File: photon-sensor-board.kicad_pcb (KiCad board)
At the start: 2 copper layers, 35 x 50 mm, 4 parts, among them U1 PHOTON, U2 DS18B20

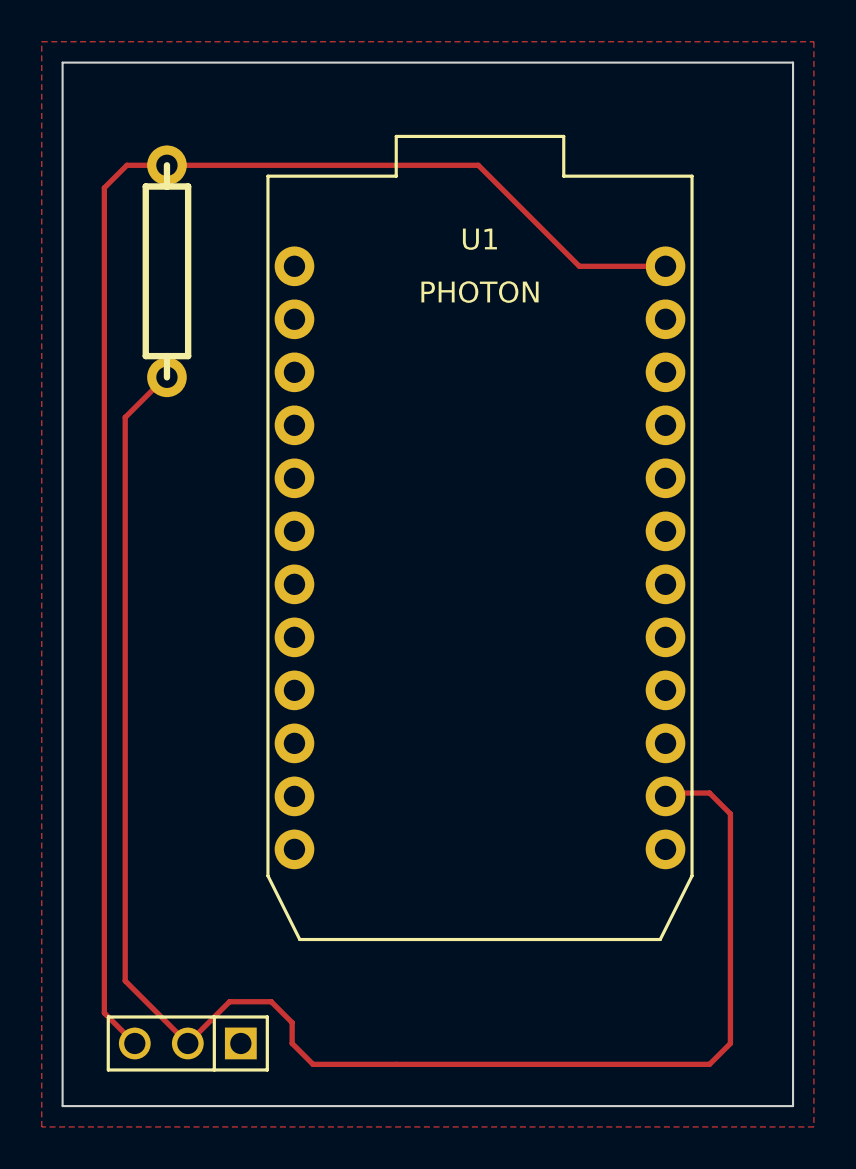
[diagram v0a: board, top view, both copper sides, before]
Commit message: Added mounting holes
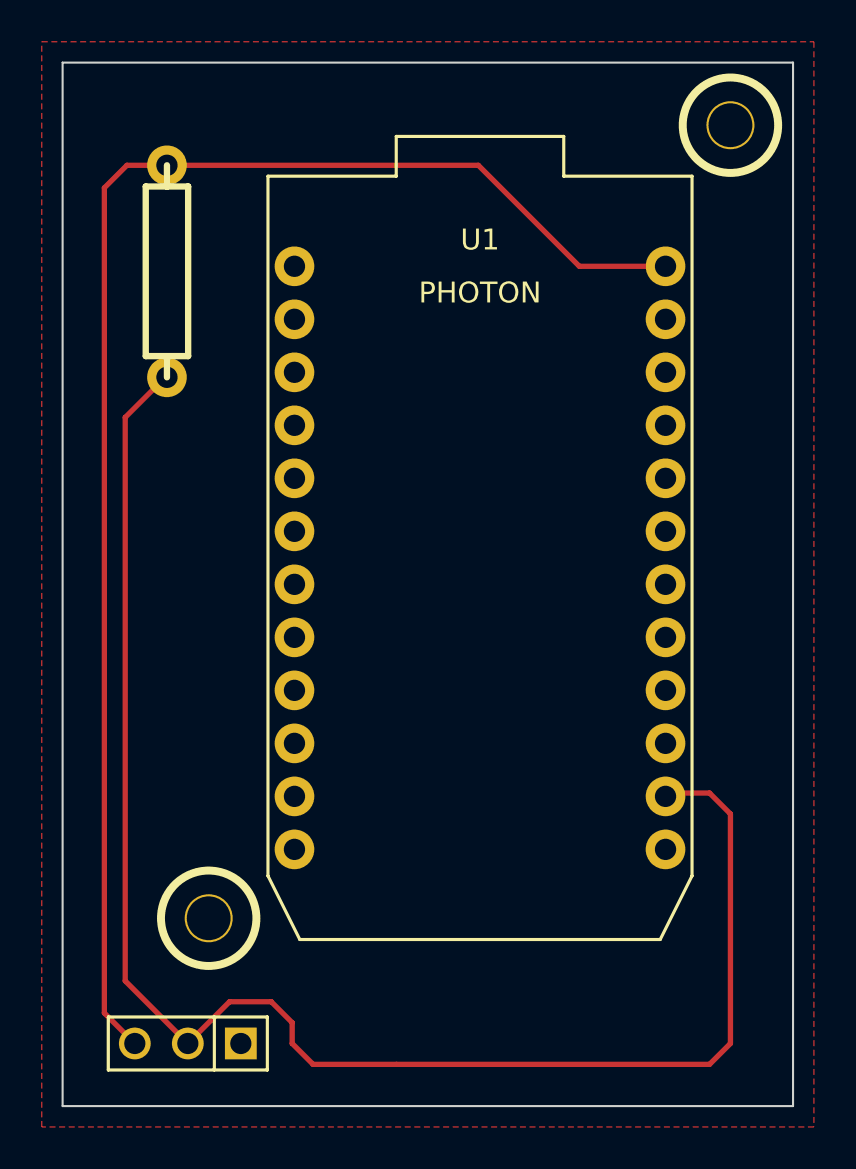
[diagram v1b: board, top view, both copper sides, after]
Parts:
- added 1PIN: P***, 1pin, F.Cu at (137.0, 98.0)
- added 1PIN: P***, 1pin, F.Cu at (112.0, 136.0)
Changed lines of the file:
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@@
     (tracks 23)
     (zones 0)
-    (modules 4)
+    (modules 6)
     (nets 4)
   )
@@
     (mod_text_size 1 1)
     (mod_text_width 0.15)
-    (pad_size 1.9 1.9)
-    (pad_drill 1.02)
+    (pad_size 2.3 2.3)
+    (pad_drill 2.1)
     (pad_to_mask_clearance 0)
     (aux_axis_origin 0 0)
@@
     )
   )
-  (gr_text "Photon Sensor Board\nv1.0 2015" (at 110.5 126.25 90) (layer F.Mask)
+  (module 1pin (layer F.Cu)
+    (at 137 98)
+    (descr "module 1 pin (ou trou mecanique de percage)")
+    (tags DEV)
+    (path 1pin)
+    (fp_text reference 1PIN (at 0 -3.048) (layer F.SilkS) hide
+      (effects (font (size 1.016 1.016) (thickness 0.254)))
+    )
+    (fp_text value P*** (at 0 2.794) (layer F.SilkS) hide
+      (effects (font (size 1.016 1.016) (thickness 0.254)))
+    )
+    (fp_circle (center 0 0) (end 0 -2.286) (layer F.SilkS) (width 0.381))
+    (pad 1 thru_hole circle (at 0 0) (size 2.3 2.3) (drill 2.1)
+      (layers *.Cu *.Mask F.SilkS)
+    )
+  )
+  (module 1pin (layer F.Cu)
+    (at 112 136)
+    (descr "module 1 pin (ou trou mecanique de percage)")
+    (tags DEV)
+    (path 1pin)
+    (fp_text reference 1PIN (at 0 -3.048) (layer F.SilkS) hide
+      (effects (font (size 1.016 1.016) (thickness 0.254)))
+    )
+    (fp_text value P*** (at 0 2.794) (layer F.SilkS) hide
+      (effects (font (size 1.016 1.016) (thickness 0.254)))
+    )
+    (fp_circle (center 0 0) (end 0 -2.286) (layer F.SilkS) (width 0.381))
+    (pad 1 thru_hole circle (at 0 0) (size 2.3 2.3) (drill 2.1)
+      (layers *.Cu *.Mask F.SilkS)
+    )
+  )
+  (gr_text "Photon Sensor Board\nv1.0 2015" (at 110.5 122.5 90) (layer F.Mask)
     (effects (font (size 1.25 1.25) (thickness 0.3)))
   )
